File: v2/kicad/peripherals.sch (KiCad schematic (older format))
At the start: 7 parts, among them P2 5k, U1 6526, U11 74ACT245, U2 W65C22SxP

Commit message: All nets verified
All nets have been verified against all design. Even though v2 is not tested yet, at least, the schematic is correct.
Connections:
- net GND: now also LCD1.16 (K); no longer LCD1.15 (A)
- net at R10.2: now also LCD1.15 (A); no longer LCD1.16 (K)
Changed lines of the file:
@@
 L power:GND #PWR0117
 U 1 1 5FB341F3
-P 7650 3150
-F 0 "#PWR0117" H 7650 2900 50  0001 C CNN
-F 1 "GND" H 7655 2977 50  0000 C CNN
-F 2 "" H 7650 3150 50  0001 C CNN
-F 3 "" H 7650 3150 50  0001 C CNN
-	1    7650 3150
+P 7800 3050
+F 0 "#PWR0117" H 7800 2800 50  0001 C CNN
+F 1 "GND" H 7805 2877 50  0000 C CNN
+F 2 "" H 7800 3050 50  0001 C CNN
+F 3 "" H 7800 3050 50  0001 C CNN
+	1    7800 3050
 	1    0    0    -1
 $EndComp
@@
 Wire Wire Line
 	7650 2450 7650 2550
-Wire Wire Line
-	7650 2850 7650 2950
-Wire Wire Line
-	7650 2950 7550 2950
-Wire Wire Line
-	7550 3050 7650 3050
-Wire Wire Line
-	7650 3050 7650 3150
 $Comp
 L power:GND #PWR0119
@@
 Wire Wire Line
 	6350 3200 6350 1300
-Wire Wire Line
-	5950 4100 7950 4100
-Wire Bus Line
-	6400 2900 6400 5050
-Wire Bus Line
-	10550 3800 10550 6450
-Wire Bus Line
-	10350 2200 10350 5250
-Wire Bus Line
-	1750 2950 1750 5050
-Wire Bus Line
-	8150 3000 8150 5050
-Wire Bus Line
-	6350 3400 6350 5350
-Wire Bus Line
-	4950 3600 4950 5250
-Wire Bus Line
-	3900 5150 3900 6500
-Wire Bus Line
-	4000 3050 4000 5250
-Wire Bus Line
-	8250 3700 8250 5150
-Wire Bus Line
-	1950 3650 1950 5350
-Wire Bus Line
-	1950 5350 1950 6500
 Connection ~ 6350 1300
 Wire Wire Line
@@
 Text Label 6000 3200 0    50   ~ 0
 ~CIARES
+Wire Wire Line
+	7550 3050 7650 3050
+Wire Wire Line
+	7650 2850 7650 3050
+Wire Wire Line
+	7550 2950 7800 2950
+Wire Wire Line
+	7800 2950 7800 3050
+Wire Wire Line
+	5950 4100 7950 4100
+Wire Bus Line
+	6400 2900 6400 5050
+Wire Bus Line
+	10550 3800 10550 6450
+Wire Bus Line
+	10350 2200 10350 5250
+Wire Bus Line
+	1750 2950 1750 5050
+Wire Bus Line
+	8150 3000 8150 5050
+Wire Bus Line
+	6350 3400 6350 5350
+Wire Bus Line
+	4950 3600 4950 5250
+Wire Bus Line
+	3900 5150 3900 6500
+Wire Bus Line
+	4000 3050 4000 5250
+Wire Bus Line
+	8250 3700 8250 5150
+Wire Bus Line
+	1950 3650 1950 5350
+Wire Bus Line
+	1950 5350 1950 6500
 $EndSCHEMATC

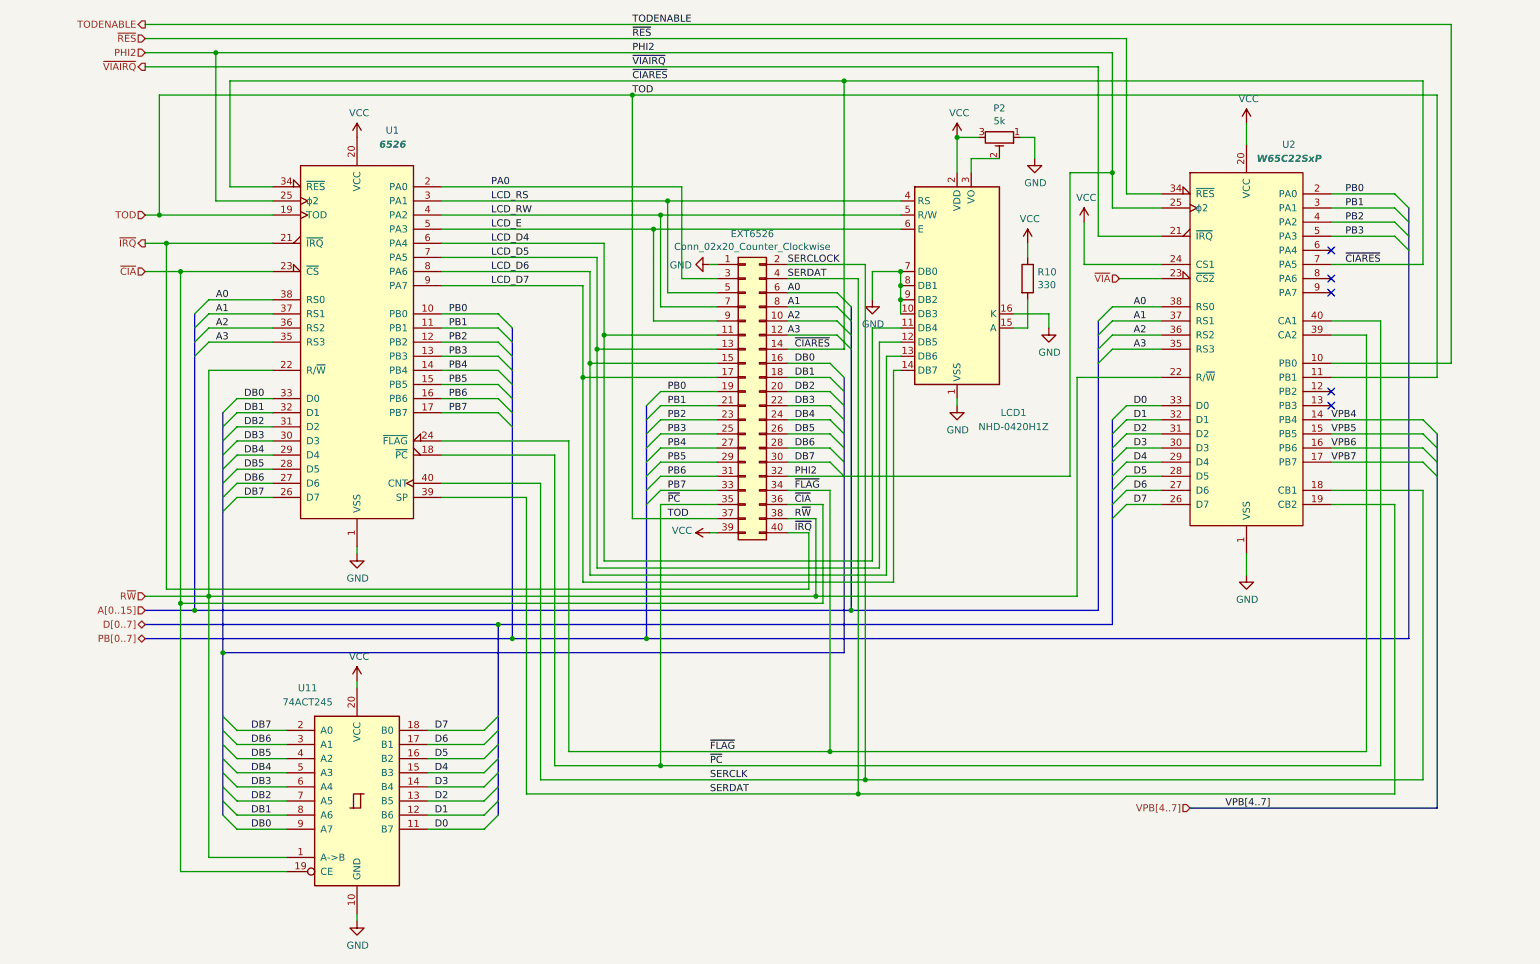
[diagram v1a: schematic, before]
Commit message: new revision - dual 6526
new revision - dual 6526
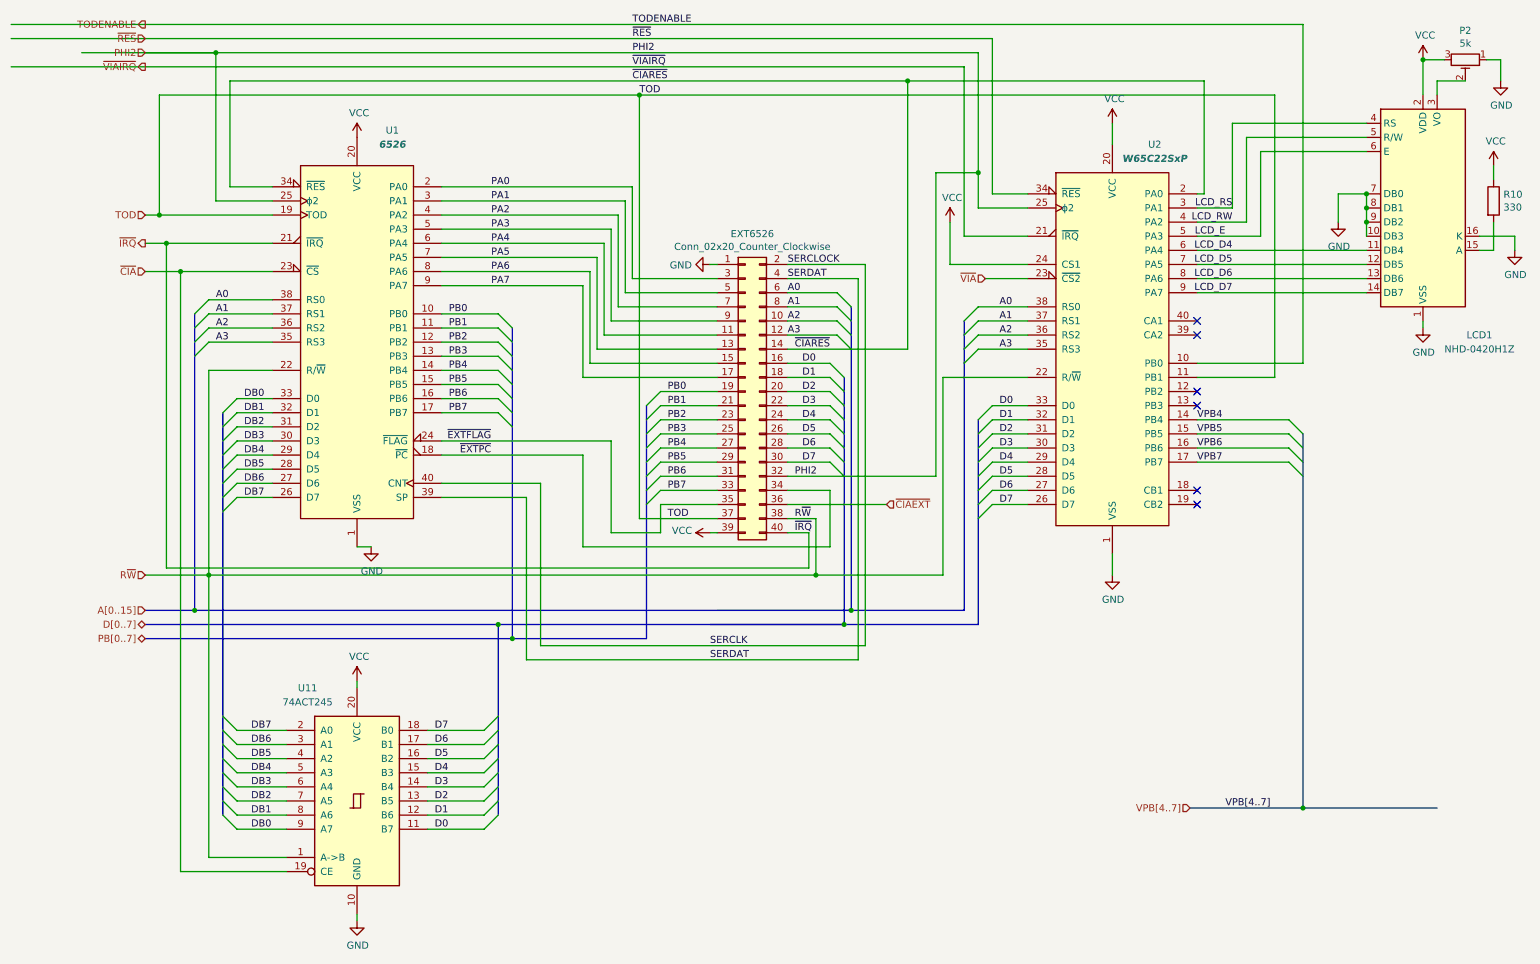
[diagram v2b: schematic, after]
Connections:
- net D0: now also EXT6526.16 (Pin_16)
- net D1: now also EXT6526.18 (Pin_18)
- net D2: now also EXT6526.20 (Pin_20)
- net D3: now also EXT6526.22 (Pin_22)
- net D4: now also EXT6526.24 (Pin_24)
- net D5: now also EXT6526.26 (Pin_26)
- net D6: now also EXT6526.28 (Pin_28)
- net D7: now also EXT6526.30 (Pin_30)
- net DB0: no longer EXT6526.16 (Pin_16)
- net DB1: no longer EXT6526.18 (Pin_18)
- net DB2: no longer EXT6526.20 (Pin_20)
- net DB3: no longer EXT6526.22 (Pin_22)
- net DB4: no longer EXT6526.24 (Pin_24)
- net DB5: no longer EXT6526.26 (Pin_26)
- net DB6: no longer EXT6526.28 (Pin_28)
- net DB7: no longer EXT6526.30 (Pin_30)
- net LCD_D4: now also U2.6 (PA4); no longer EXT6526.11 (Pin_11), U1.6 (PA4)
- net LCD_D5: now also U2.7 (PA5); no longer EXT6526.13 (Pin_13), U1.7 (PA5)
- net LCD_D6: now also U2.8 (PA6); no longer EXT6526.15 (Pin_15), U1.8 (PA6)
- net LCD_D7: now also U2.9 (PA7); no longer EXT6526.17 (Pin_17), U1.9 (PA7)
- net LCD_E: now also U2.5 (PA3); no longer EXT6526.9 (Pin_9), U1.5 (PA3)
- net LCD_RS: now also U2.3 (PA1); no longer EXT6526.5 (Pin_5), U1.3 (PA1)
- net LCD_RW: now also U2.4 (PA2); no longer EXT6526.7 (Pin_7), U1.4 (PA2)
- net PB0: no longer U2.2 (PA0)
- net PB1: no longer U2.3 (PA1)
- net PB2: no longer U2.4 (PA2)
- net PB3: no longer U2.5 (PA3)
- net SERCLK: no longer U2.18 (CB1)
- net SERDAT: no longer U2.19 (CB2)
- net ~CIA: no longer EXT6526.36 (Pin_36)
- net ~CIARES: now also U2.2 (PA0); no longer U2.7 (PA5)
- removed net ~FLAG: EXT6526.34 (Pin_34), U1.24 (~FLAG), U2.39 (CA2)
- removed net ~PC: EXT6526.35 (Pin_35), U1.18 (~PC), U2.40 (CA1)
- new net PA1: EXT6526.5 (Pin_5), U1.3 (PA1)
- new net PA2: EXT6526.7 (Pin_7), U1.4 (PA2)
- new net PA3: EXT6526.9 (Pin_9), U1.5 (PA3)
- new net PA4: EXT6526.11 (Pin_11), U1.6 (PA4)
- new net PA5: EXT6526.13 (Pin_13), U1.7 (PA5)
- new net PA6: EXT6526.15 (Pin_15), U1.8 (PA6)
- new net PA7: EXT6526.17 (Pin_17), U1.9 (PA7)
- new net ~CIAEXT: EXT6526.36 (Pin_36)
- new net ~EXTFLAG: EXT6526.35 (Pin_35), U1.24 (~FLAG)
- new net ~EXTPC: EXT6526.34 (Pin_34), U1.18 (~PC)
- no-connect marks 5 -> 6
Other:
- moved on the sheet: LCD1, P2, R10, U2
